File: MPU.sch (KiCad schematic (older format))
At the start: 40 parts, among them J1 USB_C_Receptacle, J7 Conn_01x03_Male, J8 Conn_01x03_Female, SW1 SW_Push, SW2 SW_Push, SW3 SW_Push, SW4 SW_Push, U4 W25Q16JV, U5 RP2040, Y1 445I23D12M00000

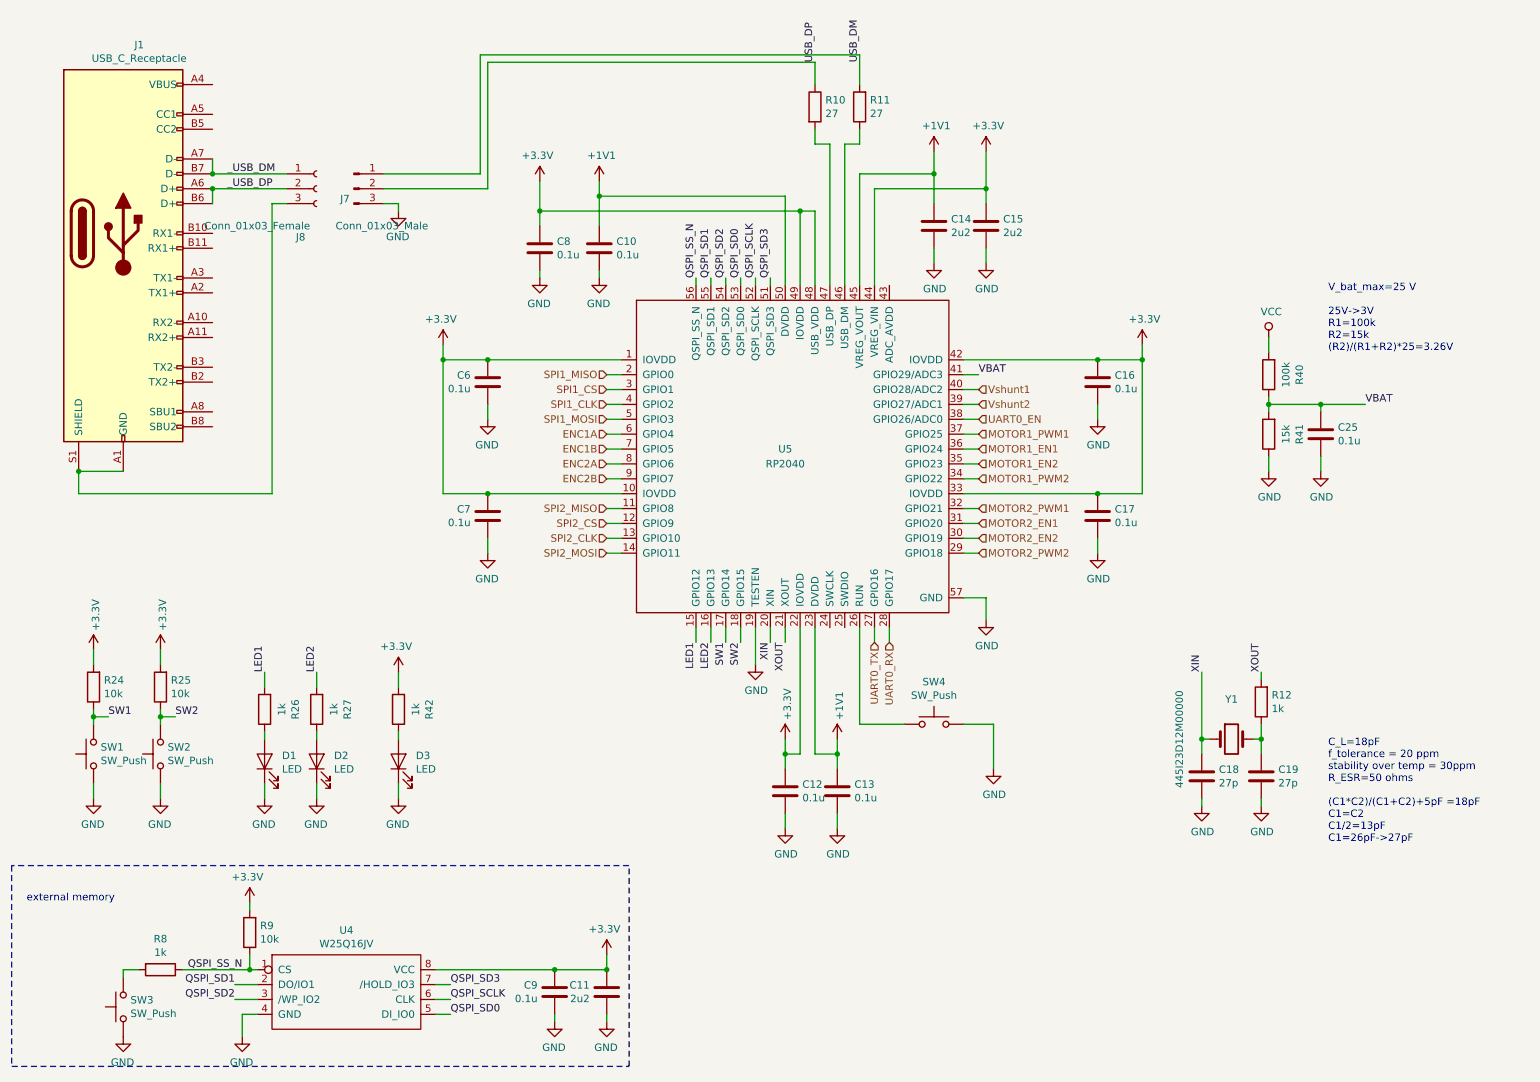
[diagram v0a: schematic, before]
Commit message: add debug pin and fix AVDD
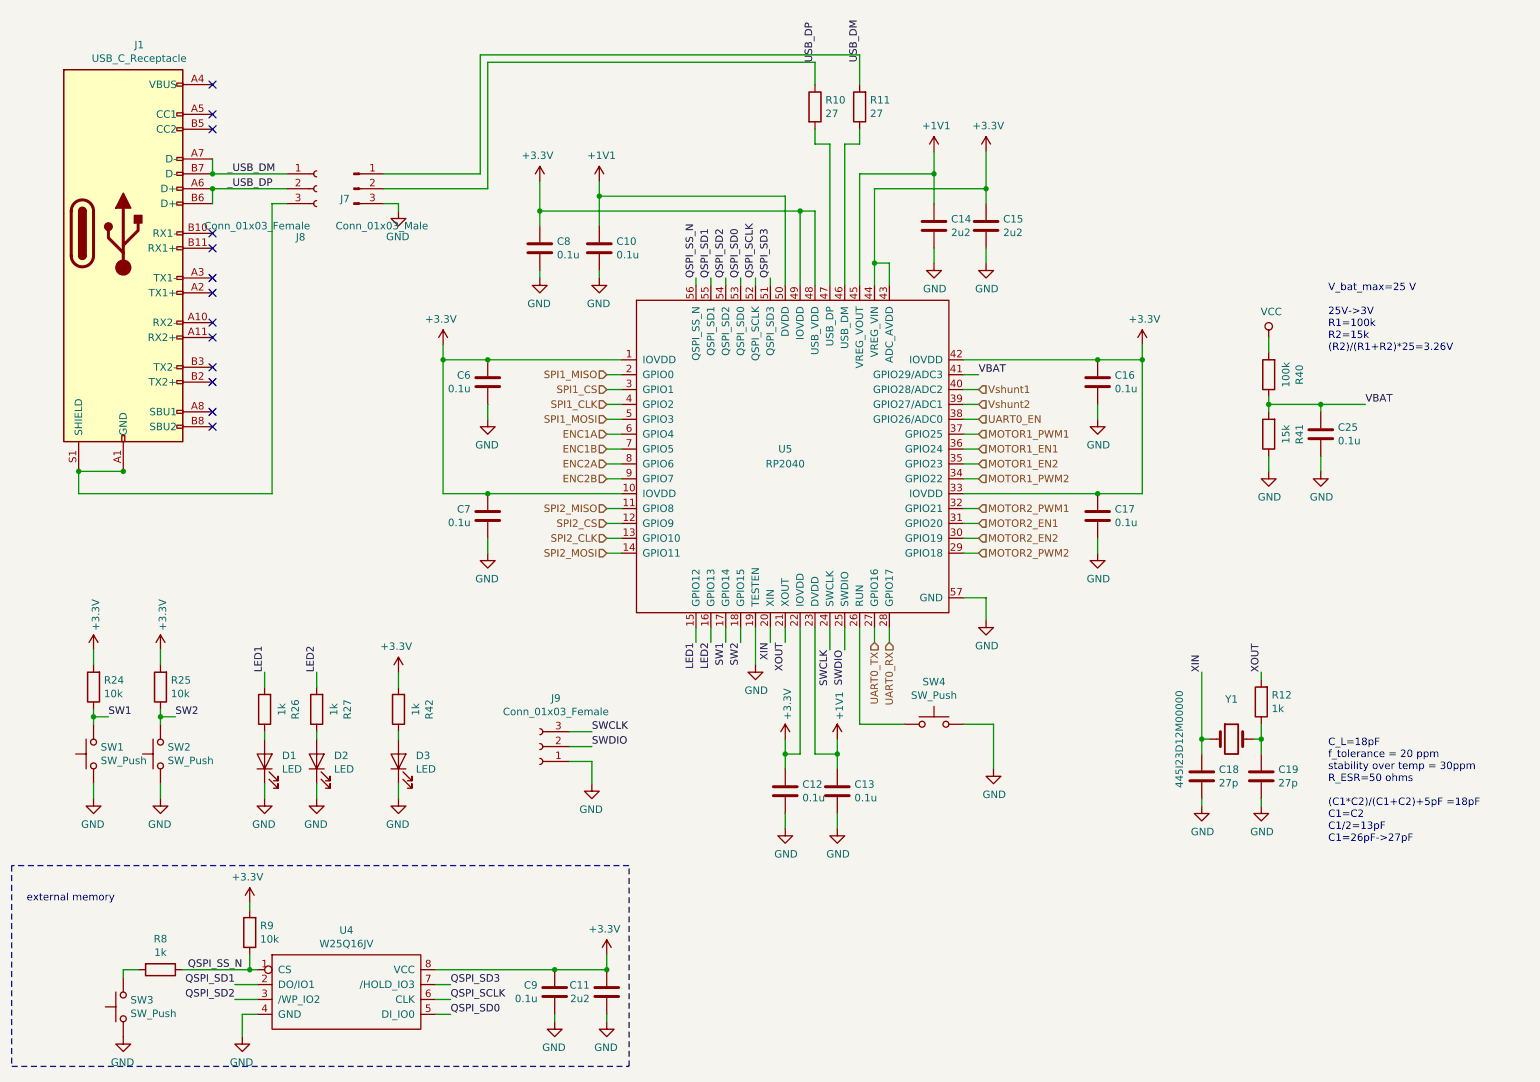
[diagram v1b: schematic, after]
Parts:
- added J9: Conn_01x03_Female, symbol Connector:Conn_01x03_Female
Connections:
- net +3V3: now also U5.43 (ADC_AVDD)
- net GND: now also J9.1 (Pin_1)
- net SWCLK: now reaches U5.24 (SWCLK)
- net SWCLK: now also J9.3 (Pin_3)
- net SWDIO: now reaches U5.25 (SWDIO)
- net SWDIO: now also J9.2 (Pin_2)
- no-connect marks 0 -> 13
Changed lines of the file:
@@
 	6300 1650 6300 2400
 Wire Wire Line
-	6400 1750 6400 2400
+	6400 1750 6400 2250
 $Comp
 L RP_MD:W25Q16JV U4
@@
 Text Notes 9450 2850 0    50   ~ 0
 V_bat_max=25 V\n\n25V->3V\nR1=100k\nR2=15k\n(R2)/(R1+R2)*25=3.26V
+Wire Wire Line
+	6500 2400 6500 2250
+Wire Wire Line
+	6500 2250 6400 2250
+Connection ~ 6400 2250
+Wire Wire Line
+	6400 2250 6400 2400
+Wire Wire Line
+	6100 4850 6100 4700
+Wire Wire Line
+	6200 4850 6200 4700
+$Comp
+L Connector:Conn_01x03_Female J9
+U 1 1 62A13952
+P 4150 5500
+F 0 "J9" H 4042 5175 50  0000 C CNN
+F 1 "Conn_01x03_Female" H 4042 5266 50  0000 C CNN
+F 2 "" H 4150 5500 50  0001 C CNN
+F 3 "~" H 4150 5500 50  0001 C CNN
+	1    4150 5500
+	-1   0    0    1
+$EndComp
+Wire Wire Line
+	4500 5400 4350 5400
+Wire Wire Line
+	4350 5500 4500 5500
+Wire Wire Line
+	4350 5600 4500 5600
+Wire Wire Line
+	4500 5600 4500 5750
+$Comp
+L power:GND #PWR0101
+U 1 1 62A33115
+P 4500 5750
+F 0 "#PWR0101" H 4500 5500 50  0001 C CNN
+F 1 "GND" H 4505 5577 50  0000 C CNN
+F 2 "" H 4500 5750 50  0001 C CNN
+F 3 "" H 4500 5750 50  0001 C CNN
+	1    4500 5750
+	-1   0    0    -1
+$EndComp
+Text Label 6100 4850 3    50   ~ 0
+SWCLK
+Text Label 6200 4850 3    50   ~ 0
+SWDIO
+Text Label 4500 5400 0    50   ~ 0
+SWCLK
+Text Label 4500 5500 0    50   ~ 0
+SWDIO
+NoConn ~ 1950 1050
+NoConn ~ 1950 1250
+NoConn ~ 1950 1350
+NoConn ~ 1950 2050
+NoConn ~ 1950 2150
+NoConn ~ 1950 2350
+NoConn ~ 1950 2450
+NoConn ~ 1950 2650
+NoConn ~ 1950 2750
+NoConn ~ 1950 2950
+NoConn ~ 1950 3050
+NoConn ~ 1950 3250
+NoConn ~ 1950 3350
+Connection ~ 1350 3650
 $EndSCHEMATC

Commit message: v1.1
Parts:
- removed R24, R25: 10k, Resistor_SMD:R_0402_1005Metric, symbol Device:R
- added R43, R44: 51k, Resistor_SMD:R_0402_1005Metric, symbol Device:R
- J9: footprint (none) -> Connector_JST:JST_PH_B3B-PH-SM4-TB_1x03-1MP_P2.00mm_Vertical
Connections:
- net GNDA: now reaches J1.A1 (GND), J1.A12 (GND), J1.B1 (GND), J1.B12 (GND), J1.S1 (SHIELD), J8.3 (Pin_3)
- net GNDA: now also R43.2, R44.2
- net at J1.A5 (CC1): now also R43.1
- net at J1.B5 (CC2): now also R44.1
- no-connect marks 13 -> 11
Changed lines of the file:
@@
 Wire Wire Line
 	1150 5850 1150 5750
-$Comp
-L Device:R R24
-U 1 1 6281A259
-P 1150 5100
-F 0 "R24" H 1080 5054 50  0000 R CNN
-F 1 "10k" H 1080 5145 50  0000 R CNN
-F 2 "Resistor_SMD:R_0402_1005Metric" V 1080 5100 50  0001 C CNN
-F 3 "~" H 1150 5100 50  0001 C CNN
-	1    1150 5100
-	-1   0    0    1
-$EndComp
-$Comp
-L Device:R R25
-U 1 1 6281A879
-P 1600 5100
-F 0 "R25" H 1530 5054 50  0000 R CNN
-F 1 "10k" H 1530 5145 50  0000 R CNN
-F 2 "Resistor_SMD:R_0402_1005Metric" V 1530 5100 50  0001 C CNN
-F 3 "~" H 1600 5100 50  0001 C CNN
-	1    1600 5100
-	-1   0    0    1
-$EndComp
-$Comp
-L power:+3.3V #PWR09
-U 1 1 6281AAB7
-P 1150 4850
-F 0 "#PWR09" H 1150 4700 50  0001 C CNN
-F 1 "+3.3V" V 1165 4978 50  0000 L CNN
-F 2 "" H 1150 4850 50  0001 C CNN
-F 3 "" H 1150 4850 50  0001 C CNN
-	1    1150 4850
-	1    0    0    -1
-$EndComp
-Wire Wire Line
-	1150 4850 1150 4950
-Wire Wire Line
-	1150 5250 1150 5300
-$Comp
-L power:+3.3V #PWR013
-U 1 1 62821F1E
-P 1600 4850
-F 0 "#PWR013" H 1600 4700 50  0001 C CNN
-F 1 "+3.3V" V 1615 4978 50  0000 L CNN
-F 2 "" H 1600 4850 50  0001 C CNN
-F 3 "" H 1600 4850 50  0001 C CNN
-	1    1600 4850
-	1    0    0    -1
-$EndComp
-Wire Wire Line
-	1600 4850 1600 4950
-Wire Wire Line
-	1600 5250 1600 5300
 Wire Wire Line
 	1150 5300 1250 5300
-Connection ~ 1150 5300
 Wire Wire Line
 	1150 5300 1150 5350
 Wire Wire Line
 	1600 5300 1700 5300
-Connection ~ 1600 5300
 Wire Wire Line
 	1600 5300 1600 5350
@@
 $EndComp
 Wire Wire Line
-	2350 1850 2450 1850
-Wire Wire Line
 	1950 1650 2450 1650
 Wire Wire Line
@@
 	1    0    0    -1
 $EndComp
-Wire Wire Line
-	1050 3800 2350 3800
-Wire Wire Line
-	2350 1850 2350 3800
 $Comp
 L Device:LED D3
@@
 F 0 "J9" H 4042 5175 50  0000 C CNN
 F 1 "Conn_01x03_Female" H 4042 5266 50  0000 C CNN
-F 2 "" H 4150 5500 50  0001 C CNN
+F 2 "Connector_JST:JST_PH_B3B-PH-SM4-TB_1x03-1MP_P2.00mm_Vertical" H 4150 5500 50  0001 C CNN
 F 3 "~" H 4150 5500 50  0001 C CNN
 	1    4150 5500
@@
 SWDIO
 NoConn ~ 1950 1050
-NoConn ~ 1950 1250
-NoConn ~ 1950 1350
 NoConn ~ 1950 2050
 NoConn ~ 1950 2150
@@
 NoConn ~ 1950 3250
 NoConn ~ 1950 3350
-Connection ~ 1350 3650
+$Comp
+L Device:R R43
+U 1 1 62AE601A
+P 2200 1250
+F 0 "R43" V 2300 1350 50  0000 L CNN
+F 1 "51k" V 2200 1200 50  0000 L CNN
+F 2 "Resistor_SMD:R_0402_1005Metric" V 2130 1250 50  0001 C CNN
+F 3 "~" H 2200 1250 50  0001 C CNN
+	1    2200 1250
+	0    -1   -1   0
+$EndComp
+$Comp
+L Device:R R44
+U 1 1 62AF9D64
+P 2200 1350
+F 0 "R44" V 2150 1450 50  0000 L CNN
+F 1 "51k" V 2200 1300 50  0000 L CNN
+F 2 "Resistor_SMD:R_0402_1005Metric" V 2130 1350 50  0001 C CNN
+F 3 "~" H 2200 1350 50  0001 C CNN
+	1    2200 1350
+	0    -1   -1   0
+$EndComp
+Wire Wire Line
+	1950 1250 2050 1250
+Wire Wire Line
+	1950 1350 2050 1350
+Wire Wire Line
+	2350 1350 2400 1350
+Wire Wire Line
+	2400 1350 2500 1350
+Wire Wire Line
+	2350 1250 2400 1250
+Wire Wire Line
+	2400 1250 2400 1350
+Connection ~ 2400 1350
+$Comp
+L power:GNDA #PWR042
+U 1 1 62B4DD8A
+P 1050 3800
+F 0 "#PWR042" H 1050 3550 50  0001 C CNN
+F 1 "GNDA" H 1055 3627 50  0000 C CNN
+F 2 "" H 1050 3800 50  0001 C CNN
+F 3 "" H 1050 3800 50  0001 C CNN
+	1    1050 3800
+	1    0    0    -1
+$EndComp
+$Comp
+L power:GNDA #PWR043
+U 1 1 62B4E2CE
+P 2250 2100
+F 0 "#PWR043" H 2250 1850 50  0001 C CNN
+F 1 "GNDA" H 2255 1927 50  0000 C CNN
+F 2 "" H 2250 2100 50  0001 C CNN
+F 3 "" H 2250 2100 50  0001 C CNN
+	1    2250 2100
+	1    0    0    -1
+$EndComp
+$Comp
+L power:GNDA #PWR044
+U 1 1 62B4E6C7
+P 2500 1350
+F 0 "#PWR044" H 2500 1100 50  0001 C CNN
+F 1 "GNDA" H 2505 1177 50  0000 C CNN
+F 2 "" H 2500 1350 50  0001 C CNN
+F 3 "" H 2500 1350 50  0001 C CNN
+	1    2500 1350
+	0    -1   -1   0
+$EndComp
+Wire Wire Line
+	2250 2100 2250 1850
+Wire Wire Line
+	2250 1850 2450 1850
 $EndSCHEMATC

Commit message: kicad5
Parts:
- U5: symbol RP_MD:RP2040 -> RP_MD-rescue:RP2040-RP_MD
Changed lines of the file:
@@
 $EndDescr
 $Comp
-L RP_MD:RP2040 U5
+L RP_MD-rescue:RP2040-RP_MD U5
 U 1 1 626F50B5
 P 5800 3600
+AR Path="/626F50B5" Ref="U5"  Part="1"
+AR Path="/625A1F17/626F50B5" Ref="U5"  Part="1"
 F 0 "U5" H 5800 3700 50  0000 C CNN
 F 1 "RP2040" H 5800 3600 50  0000 C CNN
